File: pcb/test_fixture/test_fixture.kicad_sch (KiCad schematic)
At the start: 48 parts, among them J1 UART, J2 Power Input, J3 Conn_ARM_JTAG_SWD_10, J5 GND, J6 GND, P3.3V1 

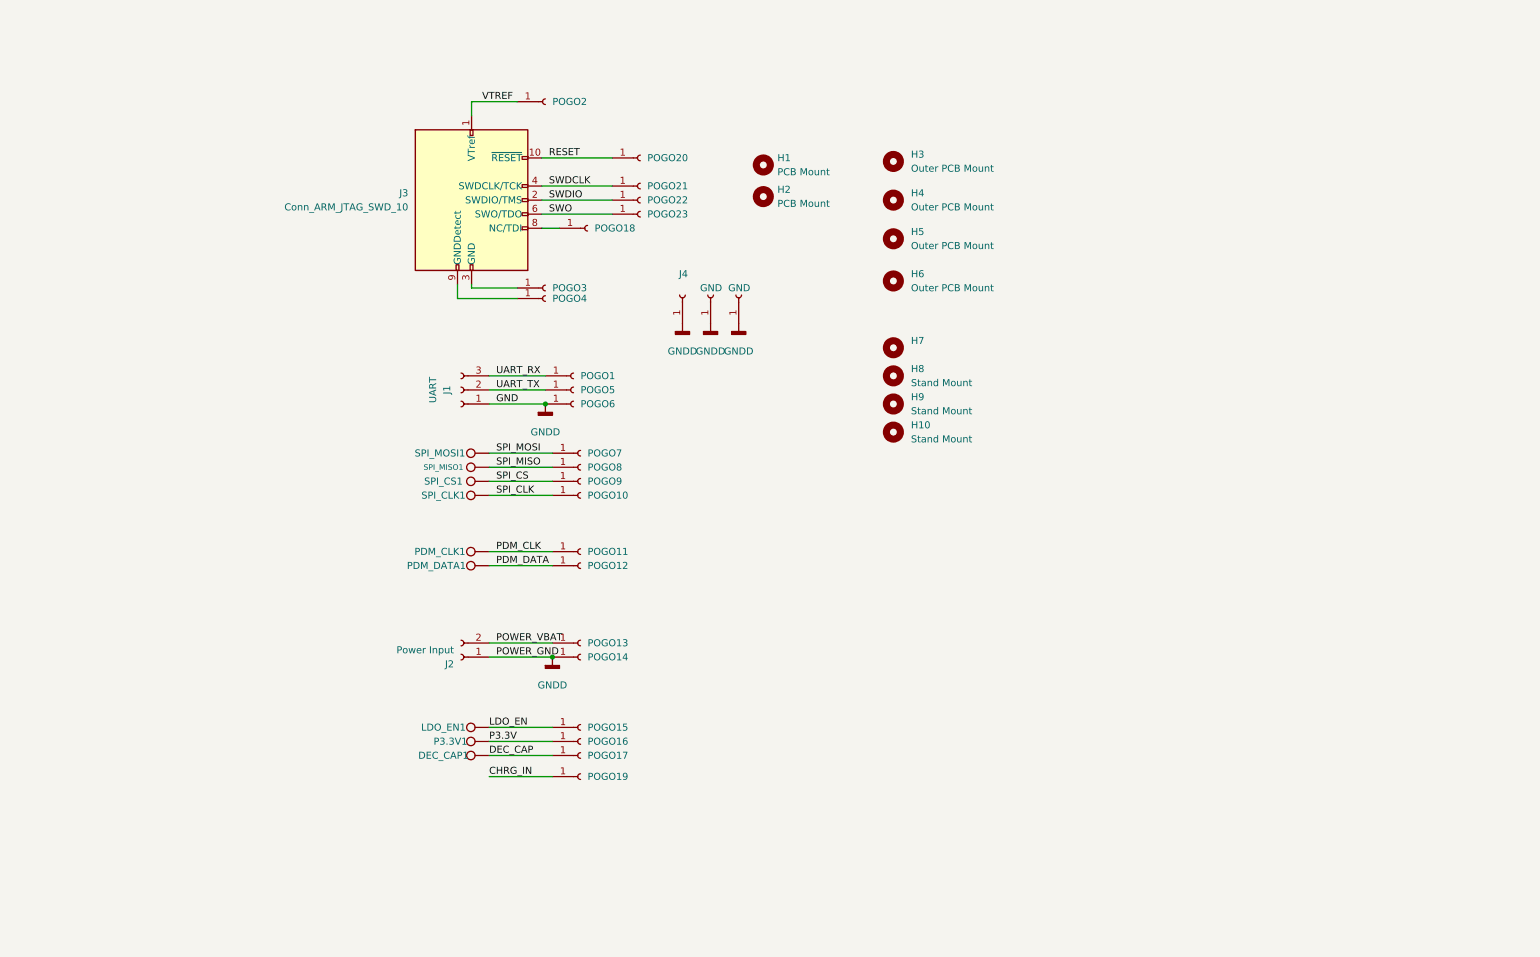
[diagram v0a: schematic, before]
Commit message: [pcb] finalized main work on fixture 1.3
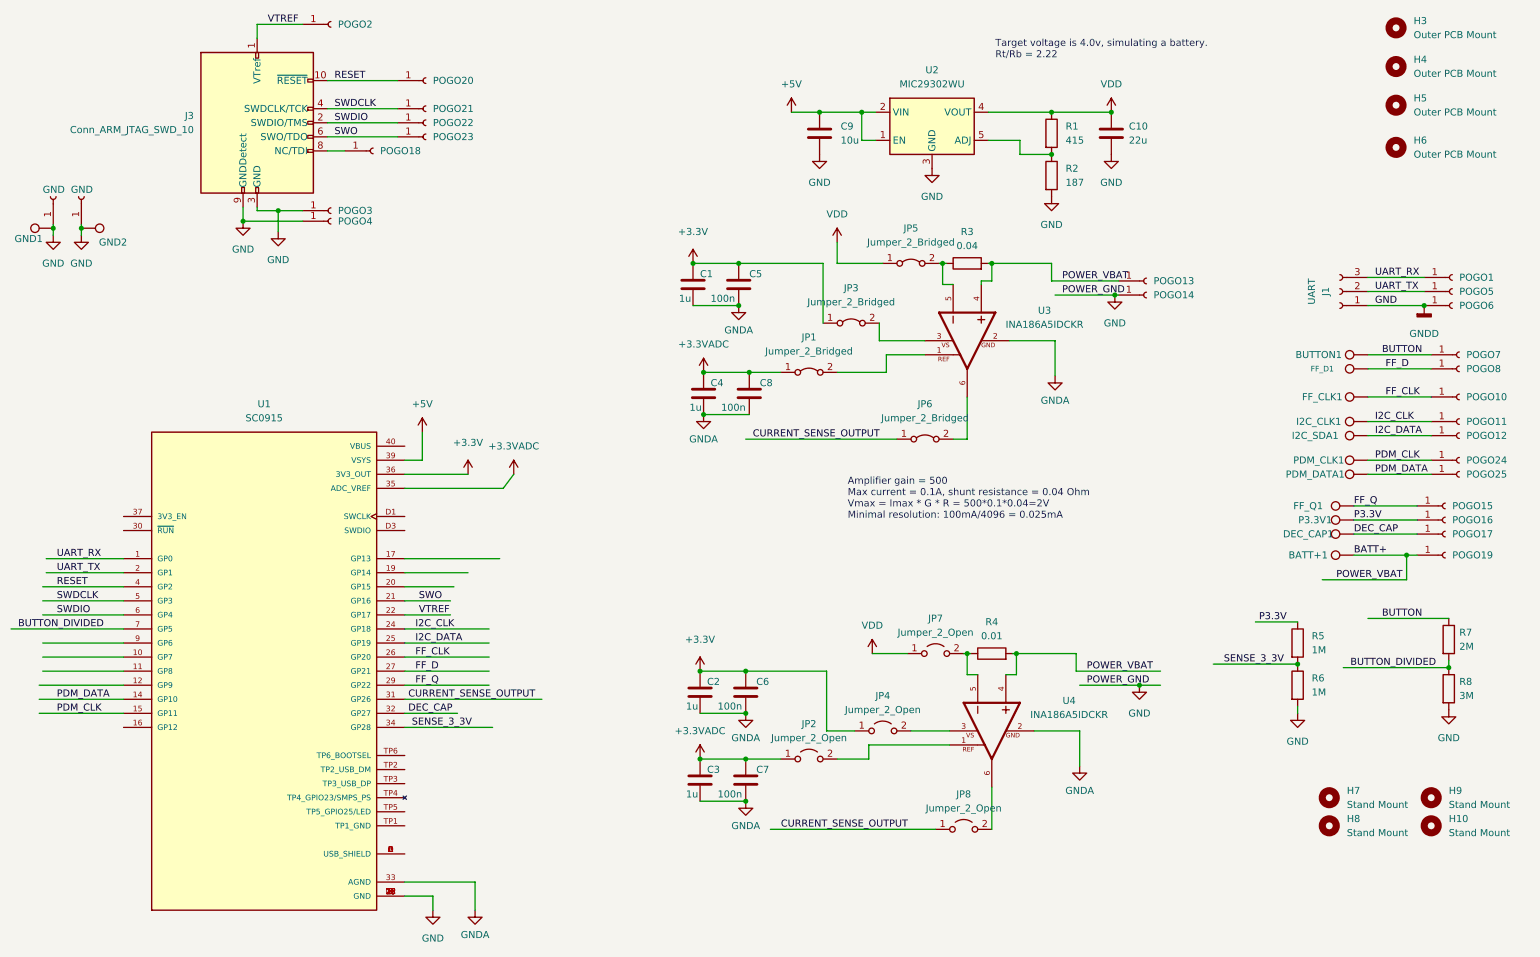
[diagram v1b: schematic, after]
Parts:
- removed H1, H2: PCB Mount, MountingHole:MountingHole_2.1mm, symbol Mechanical:MountingHole
- removed J2: Power Input, Connector_PinHeader_2.54mm:PinHeader_1x02_P2.54mm_Vertical, symbol Connector:Conn_01x02_Female
- removed J4: (no value), Connector_PinSocket_2.54mm:PinSocket_1x01_P2.54mm_Vertical, symbol Connector:Conn_01x01_Female
- removed POGO9: pogo, dictofun:POGO_PIN, symbol Connector:Conn_01x01_Female
- removed SPI_CS1: (no value), TestPoint:TestPoint_Pad_D1.5mm, symbol Connector:TestPoint
- added BATT+1, GND1, GND2, PDM_CLK1, PDM_DATA1: (no value), TestPoint:TestPoint_Pad_D1.5mm, symbol Connector:TestPoint
- added C1, C2, C3, C4: 1u, Resistor_SMD:R_1206_3216Metric, symbol Device:C
- added C10: 22u, Resistor_SMD:R_1206_3216Metric, symbol Device:C
- added C5, C6, C7, C8: 100n, Resistor_SMD:R_1206_3216Metric, symbol Device:C
- added C9: 10u, Resistor_SMD:R_1206_3216Metric, symbol Device:C
- added JP1, JP3, JP5, JP6: Jumper_2_Bridged, Jumper:SolderJumper-2_P1.3mm_Bridged2Bar_Pad1.0x1.5mm, symbol Jumper:Jumper_2_Bridged
- added JP2, JP4, JP7, JP8: Jumper_2_Open, Jumper:SolderJumper-2_P1.3mm_Open_RoundedPad1.0x1.5mm, symbol Jumper:Jumper_2_Open
- added POGO24, POGO25: pogo, fixture:POGO, symbol Connector:Conn_01x01_Female
- added R1: 415, Resistor_SMD:R_0603_1608Metric, symbol Device:R
- added R2: 187, Resistor_SMD:R_0603_1608Metric, symbol Device:R
- added R3: 0.04, Resistor_SMD:R_Shunt_Vishay_WSR2_WSR3_KelvinConnection, symbol Device:R
- added R4: 0.01, Resistor_SMD:R_Shunt_Vishay_WSR2_WSR3_KelvinConnection, symbol Device:R
- added R5, R6: 1M, Resistor_SMD:R_0603_1608Metric, symbol Device:R
- added R7: 2M, Resistor_SMD:R_0603_1608Metric, symbol Device:R
- added R8: 3M, Resistor_SMD:R_0603_1608Metric, symbol Device:R
- added U1: SC0915, MODULE_SC0915, symbol fixture:SC0915
- added U2: MIC29302WU, Package_TO_SOT_SMD:TO-263-5_TabPin3, symbol Regulator_Linear:MIC29302WU
- added U3, U4: INA186A5IDCKR, SOT65P210X110-6N, symbol fixture:INA186A1IDCKR
- H7: value (none) -> Stand Mount; footprint (none) -> MountingHole:MountingHole_2.1mm
- J5, J6: footprint Connector_PinSocket_2.54mm:PinSocket_1x01_P2.54mm_Vertical -> fixture:POGO
- POGO1, POGO10, POGO11, POGO12, POGO13, POGO14, POGO15, POGO16, POGO17, POGO18, POGO19, POGO2, POGO20, POGO21, POGO22, POGO23, POGO3, POGO4, POGO5, POGO6, POGO7, POGO8: footprint dictofun:POGO_PIN -> fixture:POGO
- renumbered SPI_MOSI1 to BUTTON1, SPI_CLK1 to FF_CLK1, SPI_MISO1 to FF_D1, LDO_EN1 to FF_Q1, PDM_CLK1 to I2C_CLK1, PDM_DATA1 to I2C_SDA1
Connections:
- net GNDD is gone; now on net GND: J1.1 (Pin_1), J5.1 (Pin_1), J6.1 (Pin_1), POGO14.1 (Pin_1), POGO6.1 (Pin_1)
- net POWER_VBAT is gone; now on net BATT+: POGO13.1 (Pin_1)
- net DEC_CAP: now also U1.32 (GP27)
- net P3.3V: now also R5.1
- net PDM_CLK: now also PDM_CLK1.1, POGO24.1 (Pin_1), U1.15 (GP11); no longer I2C_CLK1.1, POGO11.1 (Pin_1)
- net PDM_DATA: now also PDM_DATA1.1, POGO25.1 (Pin_1), U1.14 (GP10); no longer I2C_SDA1.1, POGO12.1 (Pin_1)
- net RESET: now also U1.4 (GP2)
- net SWDCLK: now also U1.5 (GP3)
- net SWDIO: now also U1.6 (GP4)
- net SWO: now also U1.21 (GP16)
- net UART_RX: now also U1.1 (GP0)
- net UART_TX: now also U1.2 (GP1)
- net VTREF: now also U1.22 (GP17)
- net GND: now reaches J3.3 (GND), J3.5 (GND), POGO3.1 (Pin_1)
- net GND: now also J3.9 (GNDDetect), POGO4.1 (Pin_1), C10.2, C9.2, GND1.1, GND2.1, R2.2, R6.2, R8.2, U1.13 (GND), U1.18 (GND), U1.23 (GND), U1.28 (GND), U1.3 (GND), U1.38 (GND), U1.8 (GND), U1.D2 (GND), U2.3 (GND)
- net CHRG_IN renamed BATT+
- net BATT+: now also BATT+1.1, R3.2, R4.2, U3.4, U4.4
- net LDO_EN renamed FF_Q
- net FF_Q: now also U1.29 (GP22)
- net SPI_CLK renamed FF_CLK
- net FF_CLK: now also U1.26 (GP20)
- net SPI_MISO renamed FF_D
- net FF_D: now also U1.27 (GP21)
- net SPI_MOSI renamed BUTTON
- net BUTTON: now also R7.1
- new net: JP2.2 (B), U4.1
- new net: JP4.2 (B), U4.3
- new net: JP7.2 (B), R4.1, U4.5
- new net: JP8.2 (B), U4.6
- new net: JP5.2 (B), R3.1, U3.5
- new net: JP1.2 (B), U3.1
- new net: R1.2, R2.1, U2.5 (ADJ)
- new net: U1.A (USB_SHIELD), U1.B (USB_SHIELD), U1.C (USB_SHIELD), U1.D (USB_SHIELD)
- new net: JP3.2 (B), U3.3
- new net: JP6.2 (B), U3.6
- new net +3.3V: C1.1, C2.1, C5.1, C6.1, JP3.1 (A), JP4.1 (A), U1.36 (3V3_OUT)
- new net +3.3VADC: C3.1, C4.1, C7.1, C8.1, JP1.1 (A), JP2.1 (A), U1.35 (ADC_VREF)
- new net +5V: C9.1, U1.39 (VSYS), U2.1 (EN), U2.2 (VIN)
- new net BUTTON_DIVIDED: R7.2, R8.1, U1.7 (GP5)
- new net CURRENT_SENSE_OUTPUT: JP6.1 (A), JP8.1 (A), U1.31 (GP26)
- new net GNDA: C1.2, C2.2, C3.2, C4.2, C5.2, C6.2, C7.2, C8.2, U1.33 (AGND), U3.2, U4.2
- new net I2C_CLK: I2C_CLK1.1, POGO11.1 (Pin_1), U1.24 (GP18)
- new net I2C_DATA: I2C_SDA1.1, POGO12.1 (Pin_1), U1.25 (GP19)
- new net SENSE_3_3V: R5.2, R6.1, U1.34 (GP28)
- new net VDD: C10.1, JP5.1 (A), JP7.1 (A), R1.1, U2.4 (VOUT)
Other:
- note added: "Amplifier gain = 500 Max current = 0.1A, shunt resistance = 0.04 Ohm Vmax = Imax * G * R = 500*0.1*0.04=2V Minimal resolution: 100mA/4096 = 0.025mA"
- note added: "Target voltage is 4.0v, simulating a battery. Rt/Rb = 2.22"
- moved on the sheet: BUTTON1, DEC_CAP1, FF_CLK1, FF_D1, FF_Q1, H10, H3, H4, H5, H6, H7, H8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

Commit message: [pcb] fixed few issues with fixture, filled in all LCSC IDs for the fixture
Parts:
- added R9: 1K, Resistor_SMD:R_0603_1608Metric, symbol Device:R
- C1, C2, C3, C4: LCSC (none) -> C14445
- C10: footprint Resistor_SMD:R_1206_3216Metric -> Capacitor_SMD:C_1206_3216Metric; LCSC (none) -> C92818
- C5, C6, C7, C8: LCSC (none) -> C113894
- C9: LCSC (none) -> C165101
- R1: LCSC (none) -> C114669
- R2: LCSC (none) -> C22828
- R5, R6: value 1M -> 100K; LCSC (none) -> C122538
- R7: value 2M -> 200K; LCSC (none) -> C118142
- R8: value 3M -> 300K; LCSC (none) -> C103526
- U2: LCSC (none) -> C11149
- U3, U4: LCSC (none) -> C2057934
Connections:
- net BUTTON: now also R9.1
- net at U1.9 (GP6): now also R9.2

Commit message: [pcb] corrected placement and bom files according to JLCPCB standards
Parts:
- C1, C2, C3, C4: LCSC C14445 -> C13832
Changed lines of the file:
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@@
       (effects (font (size 1.27 1.27)) hide)
     )
-    (property "LCSC" "C14445" (id 4) (at 137.16 154.305 0)
+    (property "LCSC" "C13832" (id 4) (at 137.16 154.305 0)
       (effects (font (size 1.27 1.27)) hide)
     )
@@
       (effects (font (size 1.27 1.27)) hide)
     )
-    (property "LCSC" "C14445" (id 4) (at 137.16 138.43 0)
+    (property "LCSC" "C13832" (id 4) (at 137.16 138.43 0)
       (effects (font (size 1.27 1.27)) hide)
     )
@@
       (effects (font (size 1.27 1.27)) hide)
     )
-    (property "LCSC" "C14445" (id 4) (at 135.89 64.77 0)
+    (property "LCSC" "C13832" (id 4) (at 135.89 64.77 0)
       (effects (font (size 1.27 1.27)) hide)
     )
@@
       (effects (font (size 1.27 1.27)) hide)
     )
-    (property "LCSC" "C14445" (id 4) (at 137.795 84.455 0)
-      (effects (font (size 1.27 1.27)) hide)
-    )
+    (property "LCSC" "C13832" (id 4) (at 137.795 84.455 0)
+      (effects (font (size 1.27 1.27)) hide)
+    )
